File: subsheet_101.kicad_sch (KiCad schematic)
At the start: 10 parts

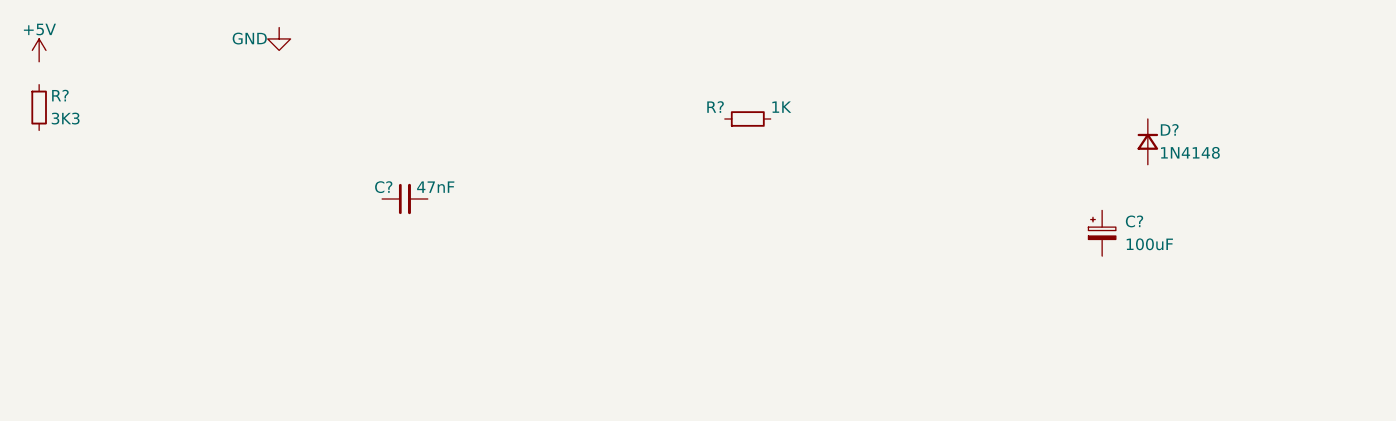
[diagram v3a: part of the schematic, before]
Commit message: bouge les composants de référence vers la feuille du pia
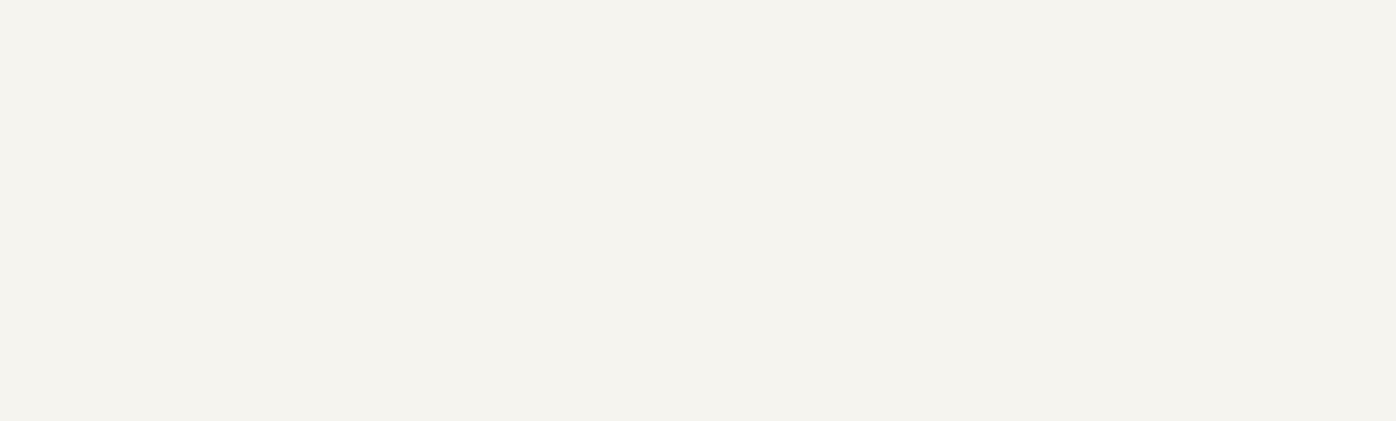
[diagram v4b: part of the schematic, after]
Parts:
- removed C?: 47nF, symbol Device:C_Small
- removed C?: 100uF, symbol Device:C_Polarized_Small
- removed D?: 1N4148, symbol Device:D_Small
- removed R?: 3K3, symbol Device:R_Small
- removed R?: 1K, symbol Device:R_Small
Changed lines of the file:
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@@
     )
-  )
-  (symbol (lib_id "Device:R_Small") (at -34.29 -26.67 0) (unit 1)
-    (in_bom yes) (on_board yes)
-    (property "Reference" "R?" (id 0) (at -33.02 -27.94 0)
-      (effects (font (size 1.27 1.27)) (justify left))
-    )
-    (property "Value" "3K3" (id 1) (at -33.02 -25.4 0)
-      (effects (font (size 1.27 1.27)) (justify left))
-    )
-    (property "Footprint" "" (id 2) (at -34.29 -26.67 0)
-      (effects (font (size 1.27 1.27)) hide)
-    )
-    (property "Datasheet" "~" (id 3) (at -34.29 -26.67 0)
-      (effects (font (size 1.27 1.27)) hide)
-    )
-    (pin "1")
-    (pin "2")
   )
   (symbol (lib_id "power:GND") (at 85.09 163.83 0) (unit 1)
@@
     (pin "1")
   )
-  (symbol (lib_id "Device:D_Small") (at 88.9 -22.86 270) (unit 1)
-    (in_bom yes) (on_board yes)
-    (property "Reference" "D?" (id 0) (at 90.17 -24.13 90)
-      (effects (font (size 1.27 1.27)) (justify left))
-    )
-    (property "Value" "1N4148" (id 1) (at 90.17 -21.59 90)
-      (effects (font (size 1.27 1.27)) (justify left))
-    )
-    (property "Footprint" "" (id 2) (at 88.9 -22.86 90)
-      (effects (font (size 1.27 1.27)) hide)
-    )
-    (property "Datasheet" "~" (id 3) (at 88.9 -22.86 90)
-      (effects (font (size 1.27 1.27)) hide)
-    )
-    (pin "1")
-    (pin "2")
-  )
   (symbol (lib_id "power:GND") (at 132.08 129.54 0) (unit 1)
     (in_bom yes) (on_board yes)
@@
     (pin "2")
   )
-  (symbol (lib_id "Device:C_Small") (at 6.35 -16.51 90) (unit 1)
-    (in_bom yes) (on_board yes)
-    (property "Reference" "C?" (id 0) (at 5.08 -17.78 90)
-      (effects (font (size 1.27 1.27)) (justify left))
-    )
-    (property "Value" "47nF" (id 1) (at 7.62 -17.78 90)
-      (effects (font (size 1.27 1.27)) (justify right))
-    )
-    (property "Footprint" "" (id 2) (at 6.35 -16.51 0)
-      (effects (font (size 1.27 1.27)) hide)
-    )
-    (property "Datasheet" "~" (id 3) (at 6.35 -16.51 0)
-      (effects (font (size 1.27 1.27)) hide)
-    )
-    (pin "1")
-    (pin "2")
-  )
-  (symbol (lib_id "power:+5V") (at -34.29 -31.75 0) (unit 1)
-    (in_bom yes) (on_board yes)
-    (property "Reference" "#PWR?" (id 0) (at -34.29 -27.94 0)
-      (effects (font (size 1.27 1.27)) hide)
-    )
-    (property "Value" "+5V" (id 1) (at -34.29 -35.306 0))
-    (property "Footprint" "" (id 2) (at -34.29 -31.75 0)
-      (effects (font (size 1.27 1.27)) hide)
-    )
-    (property "Datasheet" "" (id 3) (at -34.29 -31.75 0)
-      (effects (font (size 1.27 1.27)) hide)
-    )
-    (pin "1")
-  )
-  (symbol (lib_id "Device:C_Polarized_Small") (at 83.82 -12.7 0) (unit 1)
-    (in_bom yes) (on_board yes)
-    (property "Reference" "C?" (id 0) (at 86.36 -13.97 0)
-      (effects (font (size 1.27 1.27)) (justify left))
-    )
-    (property "Value" "100uF" (id 1) (at 86.36 -11.43 0)
-      (effects (font (size 1.27 1.27)) (justify left))
-    )
-    (property "Footprint" "" (id 2) (at 83.82 -12.7 0)
-      (effects (font (size 1.27 1.27)) hide)
-    )
-    (property "Datasheet" "~" (id 3) (at 83.82 -12.7 0)
-      (effects (font (size 1.27 1.27)) hide)
-    )
-    (pin "1")
-    (pin "2")
-  )
   (symbol (lib_id "power:GND") (at 132.08 110.49 0) (unit 1)
     (in_bom yes) (on_board yes)
@@
       (effects (font (size 1.27 1.27)) hide)
     )
-    (pin "1")
-    (pin "2")
-  )
-  (symbol (lib_id "power:GND") (at -7.62 -35.56 0) (unit 1)
-    (in_bom yes) (on_board yes)
-    (property "Reference" "#PWR?" (id 0) (at -7.62 -29.21 0)
-      (effects (font (size 1.27 1.27)) hide)
-    )
-    (property "Value" "GND" (id 1) (at -8.89 -34.29 0)
-      (effects (font (size 1.27 1.27)) (justify right))
-    )
-    (property "Footprint" "" (id 2) (at -7.62 -35.56 0)
-      (effects (font (size 1.27 1.27)) hide)
-    )
-    (property "Datasheet" "" (id 3) (at -7.62 -35.56 0)
-      (effects (font (size 1.27 1.27)) hide)
-    )
-    (pin "1")
-  )
-  (symbol (lib_id "Device:R_Small") (at 44.45 -25.4 90) (unit 1)
-    (in_bom yes) (on_board yes)
-    (property "Reference" "R?" (id 0) (at 41.91 -26.67 90)
-      (effects (font (size 1.27 1.27)) (justify left))
-    )
-    (property "Value" "1K" (id 1) (at 46.99 -26.67 90)
-      (effects (font (size 1.27 1.27)) (justify right))
-    )
-    (property "Footprint" "" (id 2) (at 44.45 -25.4 0)
-      (effects (font (size 1.27 1.27)) hide)
-    )
-    (property "Datasheet" "~" (id 3) (at 44.45 -25.4 0)
-      (effects (font (size 1.27 1.27)) hide)
-    )

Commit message: commence PIA
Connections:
- net RxW renamed R/~{W}
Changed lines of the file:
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@@
     )
   )
-  (global_label "RxW" (shape input) (at 132.08 116.84 0) (fields_autoplaced)
+  (global_label "R{slash}~{W}" (shape input) (at 132.08 116.84 0) (fields_autoplaced)
     (effects (font (size 1.27 1.27)) (justify left))
-    (property "Intersheet References" "${INTERSHEET_REFS}" (id 0) (at 138.2426 116.7606 0)
+    (property "Intersheet References" "${INTERSHEET_REFS}" (id 0) (at 138.545 116.7606 0)
       (effects (font (size 1.27 1.27)) (justify left) hide)
     )

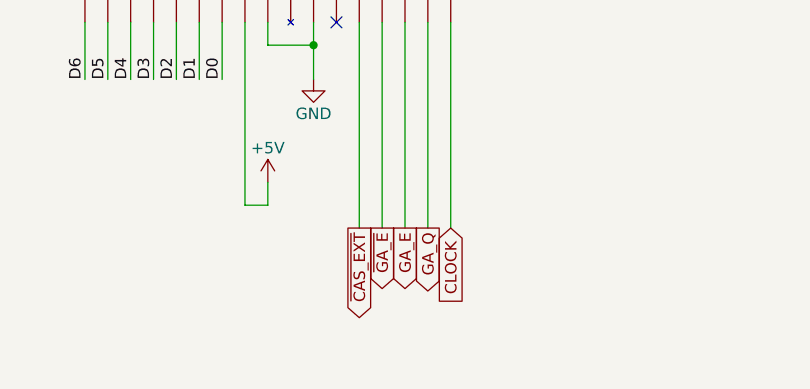
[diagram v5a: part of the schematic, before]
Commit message: rename GA_E/GA_Q/~{GA_E} into E/Q/~{E}
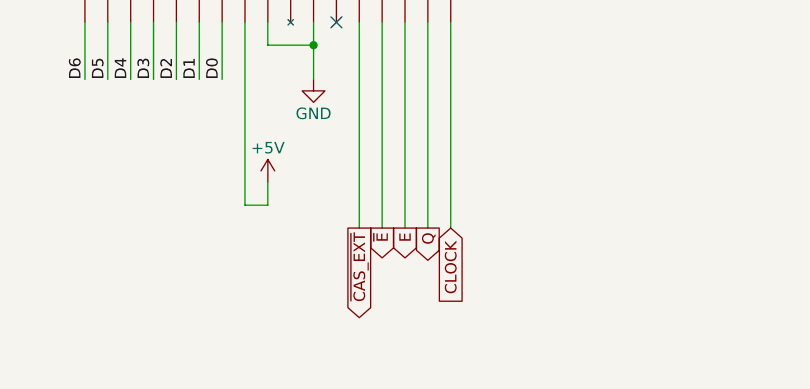
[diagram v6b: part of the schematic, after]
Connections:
- net GA_E renamed E
- net GA_Q renamed Q
- net ~{GA_E} renamed ~{E}
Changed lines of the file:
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@@
     )
   )
-  (global_label "GA_Q" (shape output) (at 97.79 180.34 270) (fields_autoplaced)
+  (global_label "Q" (shape output) (at 97.79 180.34 270) (fields_autoplaced)
     (effects (font (size 1.27 1.27)) (justify right))
-    (property "Intersheet References" "${INTERSHEET_REFS}" (id 0) (at 97.7106 187.4098 90)
+    (property "Intersheet References" "${INTERSHEET_REFS}" (id 0) (at 97.7106 184.0836 90)
       (effects (font (size 1.27 1.27)) (justify right) hide)
     )
@@
     )
   )
-  (global_label "~{GA_E}" (shape output) (at 92.71 180.34 270) (fields_autoplaced)
+  (global_label "~{E}" (shape output) (at 92.71 180.34 270) (fields_autoplaced)
     (effects (font (size 1.27 1.27)) (justify right))
-    (property "Intersheet References" "${INTERSHEET_REFS}" (id 0) (at 92.6306 187.2283 90)
+    (property "Intersheet References" "${INTERSHEET_REFS}" (id 0) (at 92.6306 183.9021 90)
       (effects (font (size 1.27 1.27)) (justify right) hide)
     )
@@
     )
   )
-  (global_label "GA_E" (shape output) (at 95.25 180.34 270) (fields_autoplaced)
+  (global_label "E" (shape output) (at 95.25 180.34 270) (fields_autoplaced)
     (effects (font (size 1.27 1.27)) (justify right))
-    (property "Intersheet References" "${INTERSHEET_REFS}" (id 0) (at 95.1706 187.2283 90)
+    (property "Intersheet References" "${INTERSHEET_REFS}" (id 0) (at 95.1706 183.9021 90)
       (effects (font (size 1.27 1.27)) (justify right) hide)
     )

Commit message: remise au propre
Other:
- title: Conversion du Thomson MO5 — Unité centrale -> Conversion du Thomson MO5 — Unité centrale v1
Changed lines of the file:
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@@
   (paper "A4" portrait)
   (title_block
-    (title "Conversion du Thomson MO5 — Unité centrale")
-    (date "2023-05-12")
+    (title "Conversion du Thomson MO5 — Unité centrale v1")
+    (date "2023-05-14")
     (rev "DRAFT")
     (comment 1 "http://github.com/sporniket/kicad-conversions--thomson-mo5--v1")
-    (comment 2 "Dépôt d'origine : ")
+    (comment 3 "Gate Array Motorola MCA 1300 ALS")
     (comment 4 "Reference : POP5001 501994-01")
   )

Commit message: début des horloges
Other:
- note added: "De I16-8"
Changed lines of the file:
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@@
+    (effects (font (size 1.27 1.27)) (justify left bottom))
+  )
+  (text "De I16-8" (at 135.89 102.87 0)
     (effects (font (size 1.27 1.27)) (justify left bottom))
   )
@@
     )
   )
-  (global_label "SYCL" (shape output) (at 128.27 101.6 0) (fields_autoplaced)
+  (global_label "SYCL" (shape input) (at 128.27 101.6 0) (fields_autoplaced)
     (effects (font (size 1.27 1.27)) (justify left))
     (property "Intersheet References" "${INTERSHEET_REFS}" (id 0) (at 135.2793 101.5206 0)
@@
     )
   )
-  (global_label "H16" (shape output) (at 128.27 96.52 0) (fields_autoplaced)
+  (global_label "H16" (shape input) (at 128.27 96.52 0) (fields_autoplaced)
     (effects (font (size 1.27 1.27)) (justify left))
     (property "Intersheet References" "${INTERSHEET_REFS}" (id 0) (at 134.4326 96.4406 0)
